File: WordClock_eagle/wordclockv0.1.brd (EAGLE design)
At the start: 100 x 80 mm, 38 parts, among them IC1 TLC5925, Q1 8MHz, Q2 32.768kHz, U1 MBT3906DW1T1G, U2 MBT3906DW1T1G, U3 MBT3906DW1T1G, U4 MBT3906DW1T1G, U5 MBT3906DW1T1G

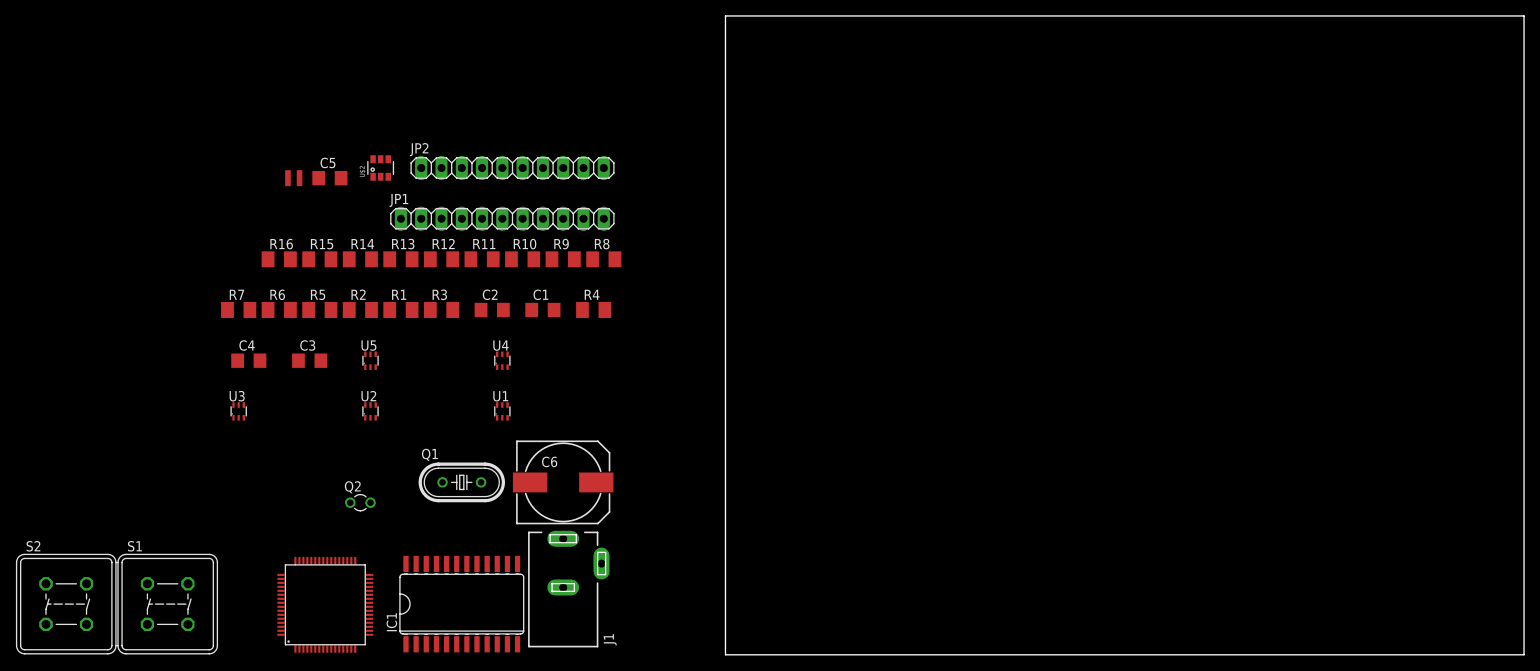
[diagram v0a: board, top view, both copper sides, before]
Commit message: Did the board. Rough draft without consideration for manufacturing
Fabricating this thing is going to be hell :imp:
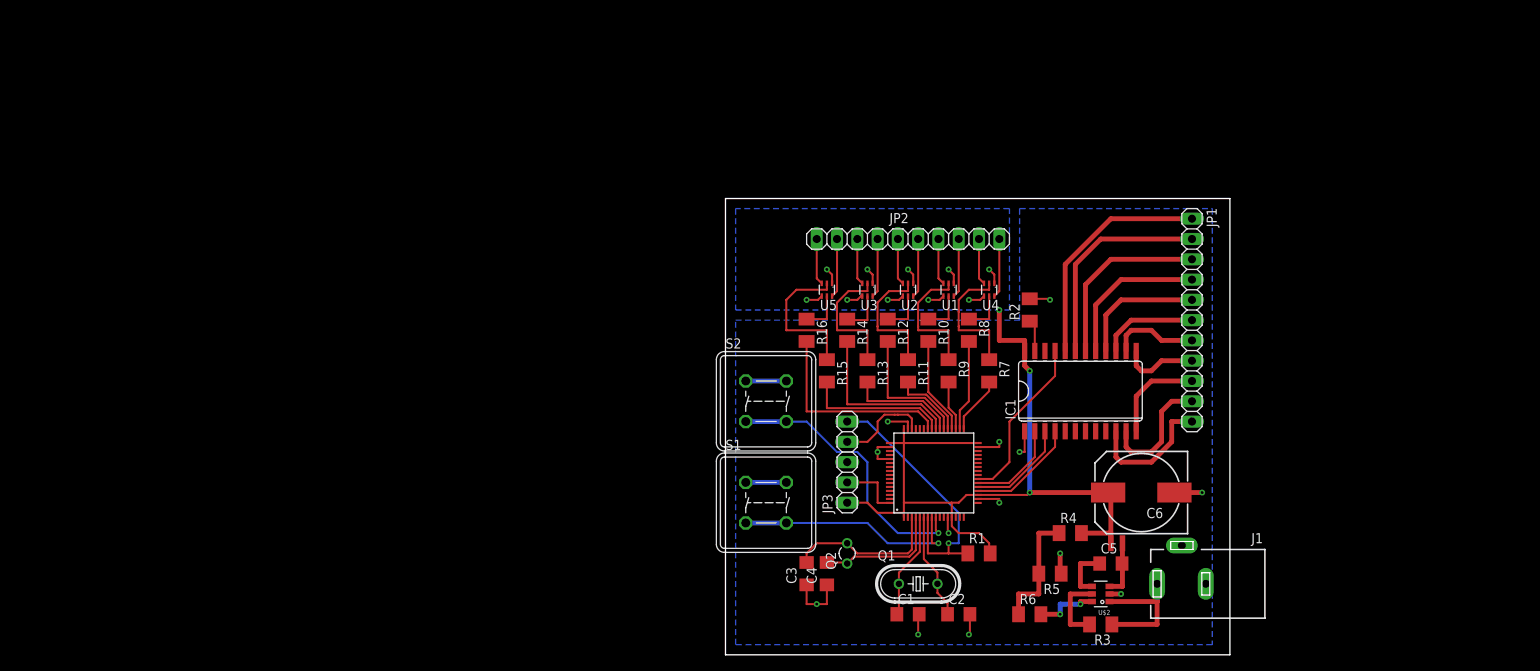
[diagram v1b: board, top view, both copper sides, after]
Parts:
- added JP3: (no value), pinhead:1X05
- moved U$3 111.4 mm to (48.3, 14.0), turned to 180 degrees
- moved C5 109.1 mm to (48.3, 11.4)
- moved U$2 104.8 mm to (47.0, 7.62), turned to 90 degrees
- moved R6 101.4 mm to (38.1, 5.08)
- moved R5 97.2 mm to (40.6, 10.2), turned to 180 degrees
- moved R7 94.3 mm to (33.0, 35.6), turned to 270 degrees
- moved R3 91.5 mm to (47.0, 3.81), turned to 180 degrees
- moved S2 91.2 mm to (5.08, 31.8)
- moved JP1 87.3 mm to (58.4, 41.9), turned to 270 degrees
- moved R2 83.8 mm to (38.1, 43.2), turned to 90 degrees
- moved IC1 81.9 mm to (44.5, 33.0)
- moved U3 80.2 mm to (17.8, 45.7), turned to 180 degrees
- moved R1 78.5 mm to (31.8, 12.7)
- moved U$1 78.0 mm to (25.4, 22.9)
- moved J1 77.5 mm to (57.1, 8.89), turned to 90 degrees
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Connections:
- removed net N$8: C6.-, J1.2, J1.3, R5.1, U$2.P$2
- net GND: now also C6.-, J1.2, J1.3, JP3.3, R5.1, S1.2, S2.2, U$2.P$2
- net LE: now also U$1.20; no longer U$1.22
- net N$16: now also S1.4
- net N$20: now also S2.4
- net NRST: now also JP3.5
- net SDI: now also U$1.22; no longer U$1.20
- net SWDCLK: now also JP3.2
- net SWDIO: now also JP3.4
- net VDD: now also JP3.1
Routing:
- net VDD: track 0.00 -> 122.7 mm, vias 0 -> 13
- net GND: track 0.00 -> 53.0 mm, vias 0 -> 13
- net N$20: track 0.00 -> 35.1 mm, vias 0 -> 1
- net NRST: track 0.00 -> 34.6 mm, vias 0 -> 1
- net N$16: track 0.00 -> 29.3 mm, vias 0 -> 1
- net N$24: track 0.00 -> 29.1 mm
- net N$25: track 0.00 -> 26.8 mm
- net LCOL10: track 0.00 -> 25.4 mm
- net N$26: track 0.00 -> 23.0 mm
- net !OE: track 0.00 -> 21.1 mm
- net LCOL8: track 0.00 -> 21.0 mm
- net N$4: track 0.00 -> 19.7 mm
- net N$27: track 0.00 -> 19.1 mm
- net N$39: track 0.00 -> 19.0 mm
- net LCOL9: track 0.00 -> 18.2 mm
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- added copper zone on layer 16, net GND
- added copper zone on layer 16, net VDD
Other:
- board size 100 x 80 mm -> 63.2 x 57.1 mm
